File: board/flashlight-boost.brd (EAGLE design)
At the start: 15 x 25 mm, 15 parts

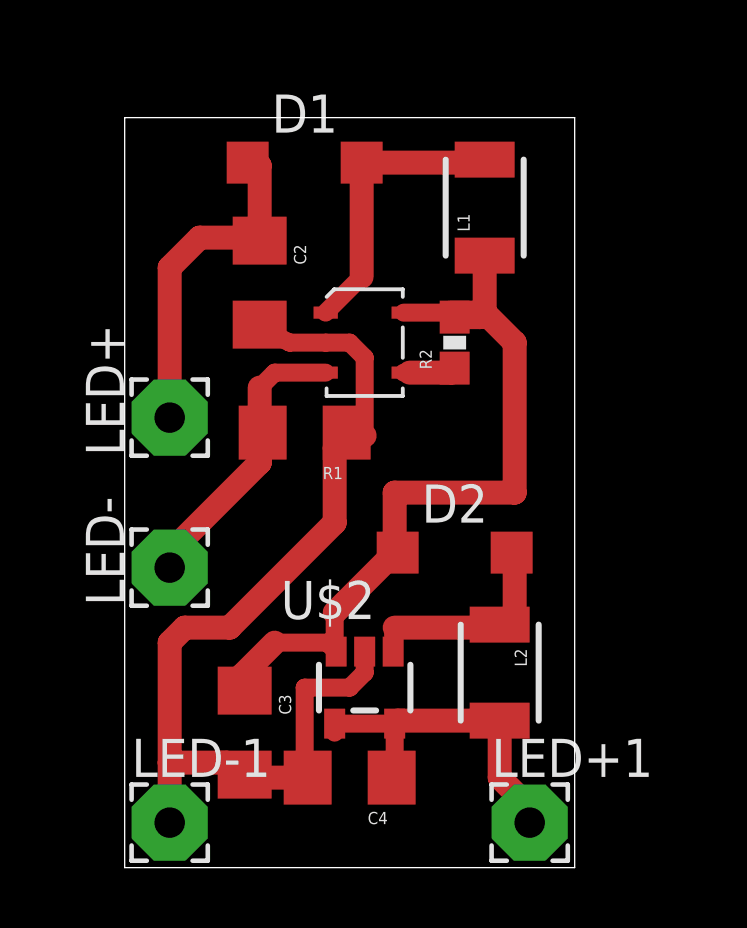
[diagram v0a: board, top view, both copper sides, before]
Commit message: removing constant current LED driver since the current sense resistor for it is the same value as the LED series resistor
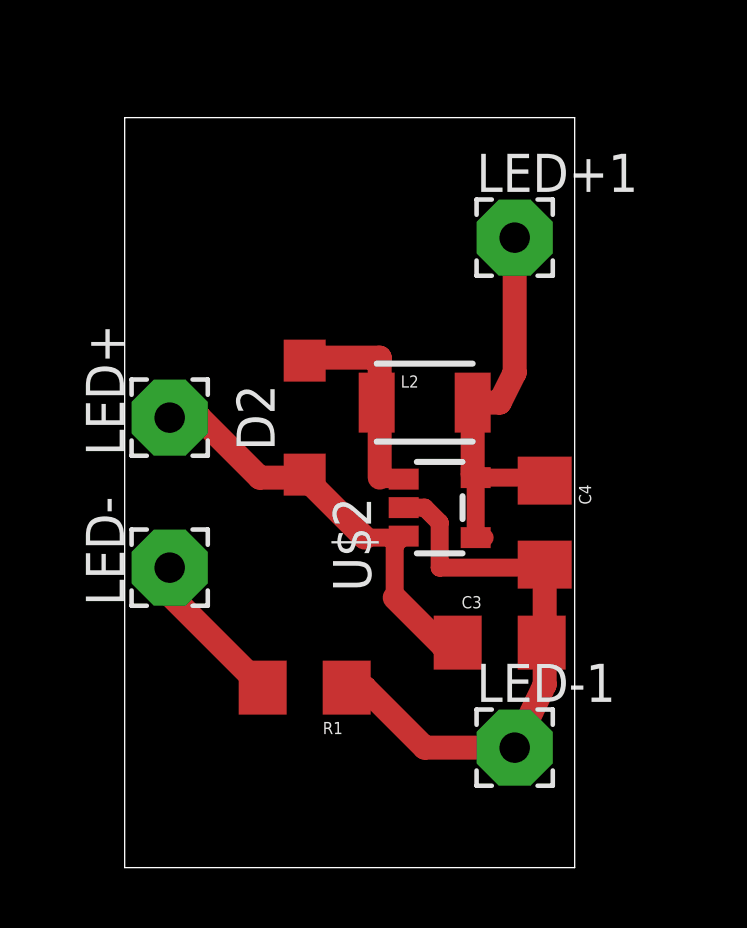
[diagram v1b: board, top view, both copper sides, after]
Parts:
- removed C2: 2.2uF/25v, SparkFun-Passives:1206
- removed D1: MBR0530, diode:SOD123
- removed L1: 10uF/1.2A, SparkFun-Passives:1210
- removed R2: 100k, SparkFun-Resistors:0603-RES
- removed U$1: LM3410-SOT-23-5, Synapseware:SOT-23-5
- R1: value 6.5 -> 4R3
- moved LED+1 19.5 mm to (13.0, 21.0)
- moved LED-1 11.8 mm to (13.0, 4.00)
- moved C4 10.7 mm to (14.0, 11.5), turned to 270 degrees
- moved L2 9.34 mm to (10.0, 15.5), turned to 0 degrees
- moved C3 9.01 mm to (12.5, 7.50), turned to 0 degrees
- moved R1 8.50 mm to (6.00, 6.00)
- moved D2 6.73 mm to (6.00, 15.0), turned to 90 degrees
- moved U$2 6.50 mm to (10.5, 12.0), turned to 90 degrees
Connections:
- removed net DIM: R2.1, U$1.4
- removed net N$10: C2.1, D1.C, LED+.1
- removed net N$2: D1.A, L1.2, U$1.1
- net GND: no longer C2.2, U$1.2
- net N$7: no longer U$1.3
- net VSUPPLY: now also LED+.1; no longer L1.1, R2.2, U$1.5
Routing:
- net GND: track 35.4 -> 19.9 mm
- net VSUPPLY: track 26.9 -> 14.7 mm
- net N$10: track 11.4 -> 0.00 mm
- net N$2: track 9.61 -> 0.00 mm
- net N$7: track 10.7 -> 5.28 mm
- net DIM: track 1.78 -> 0.00 mm
- net VCC: track 12.3 -> 13.7 mm

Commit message: misc updates
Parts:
- L2: value 12uH -> 22uH
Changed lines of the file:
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@@
 <setting verticaltext="up"/>
 </settings>
-<grid distance="0.5" unitdist="mm" unit="mm" style="lines" multiple="1" display="yes" altdistance="0.1" altunitdist="mm" altunit="mm"/>
+<grid distance="0.05" unitdist="inch" unit="inch" style="lines" multiple="1" display="yes" altdistance="0.005" altunitdist="inch" altunit="inch"/>
 <layers>
 <layer number="1" name="Top" color="4" fill="1" visible="yes" active="yes"/>
@@
 <element name="LED-1" library="wirepad" package="2,54/1,0" value="GND" x="13" y="4"/>
 <element name="U$2" library="Sipex Custom" package="SOT23-5" value="SP6641SP6641A/B" x="10.5" y="12" rot="R90"/>
-<element name="L2" library="SparkFun-Passives" package="1210" value="12uH" x="10" y="15.5"/>
+<element name="L2" library="SparkFun-Passives" package="1210" value="22uH" x="10" y="15.5"/>
 <element name="D2" library="diode" package="SOD123" value="MBR0530" x="6" y="15" rot="R90"/>
 <element name="C3" library="SparkFun-Passives" package="1206" value="22uF" x="12.5" y="7.5"/>

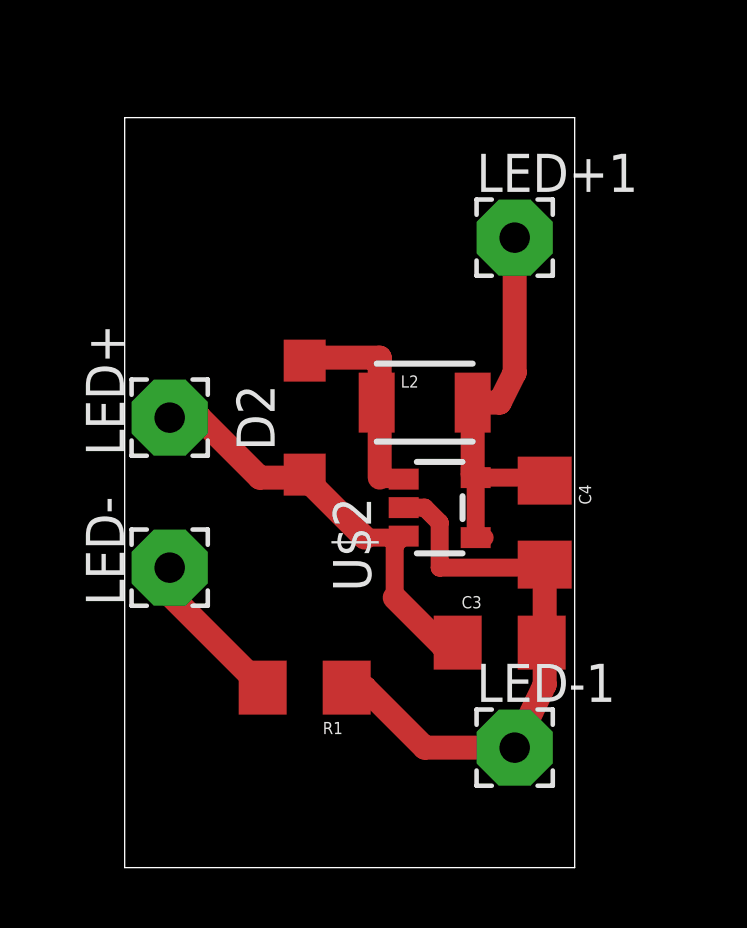
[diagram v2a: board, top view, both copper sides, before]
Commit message: Converting driver board to use LTC3490 part
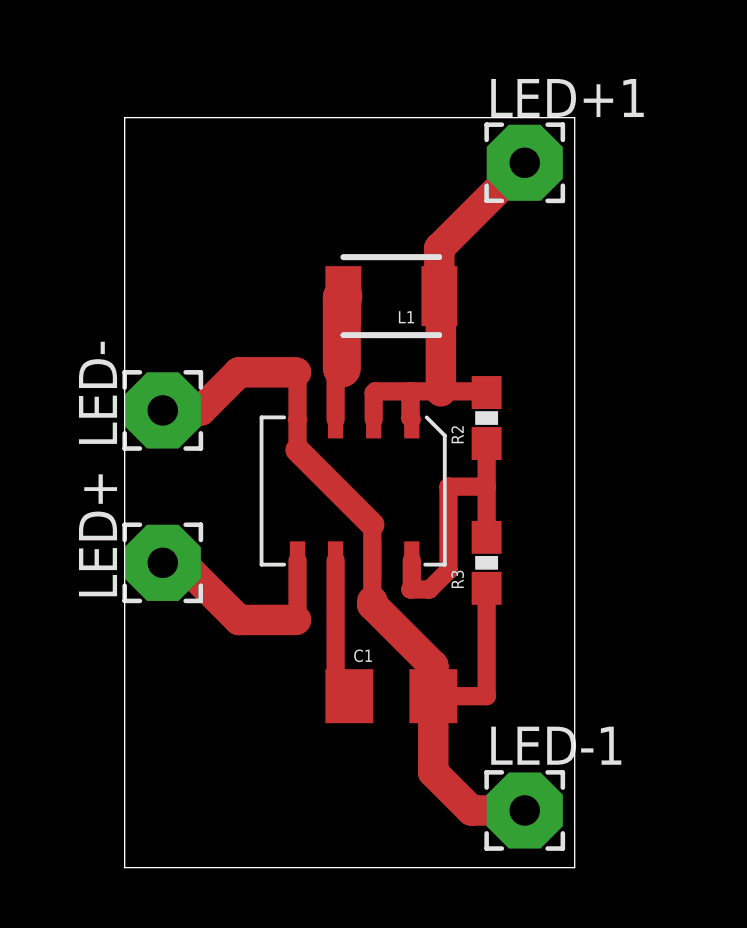
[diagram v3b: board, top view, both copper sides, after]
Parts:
- removed C3, C4: 22uF, SparkFun-Passives:1206
- removed D2: MBR0530, diode:SOD123
- removed L2: 22uH, SparkFun-Passives:1210
- removed R1: 4R3, SparkFun-Resistors:1206
- removed U$2: SP6641SP6641A/B, Sipex Custom:SOT23-5
- added C1: 4.7uF/XR7, SparkFun-Passives:1206
- added L1: 4.7uH, SparkFun-Passives:1210
- added R2: 300k, SparkFun-Resistors:0603-RES
- added R3: 100k, SparkFun-Resistors:0603-RES
- added U$1: LTC3490NSOIC-8, Synapseware:NSOIC-8
- moved LED- 5.25 mm to (1.27, 15.2)
- moved LED+ 4.85 mm to (1.27, 10.2)
- moved LED+1 2.52 mm to (13.3, 23.5)
- moved LED-1 2.12 mm to (13.3, 1.91)
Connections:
- removed net N$7: LED-.1, R1.2
- removed net N$9: D2.A, L2.1, U$2.1
- removed net VSUPPLY: C3.1, D2.C, LED+.1, U$2.3
- new net LED: LED+.1, U$1.5
- new net N$10: R2.1, R3.2, U$1.8
- new net N$4: L1.2, U$1.3
- new net N$5: C1.1, U$1.6
- new net N$6: U$1.7
- net GND: now also C1.2, LED-.1, R3.1, U$1.4; no longer C3.2, C4.2, R1.1, U$2.2
- net VCC: now also L1.1, R2.2, U$1.1, U$1.2; no longer C4.1, L2.2, U$2.4, U$2.5
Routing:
- net VSUPPLY: track 14.7 -> 0.00 mm
- net GND: track 19.9 -> 29.7 mm
- net N$10: track 0.00 -> 9.71 mm
- net N$9: track 7.97 -> 0.00 mm
- net LED: track 0.00 -> 7.24 mm
- net N$7: track 5.28 -> 0.00 mm
- net N$5: track 0.00 -> 5.19 mm
- net N$4: track 0.00 -> 4.22 mm
- net VCC: track 13.7 -> 14.5 mm
